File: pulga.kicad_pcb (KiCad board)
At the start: 2 copper layers, 12 parts

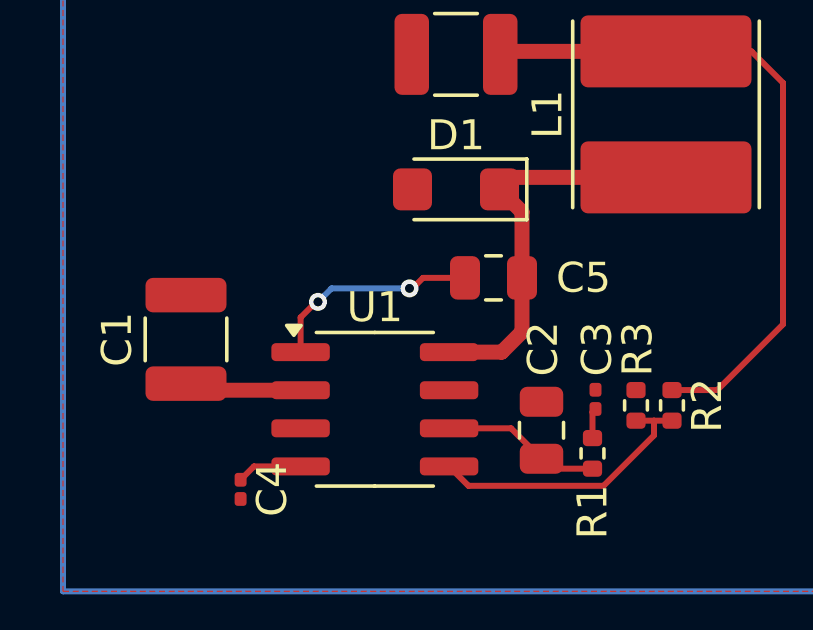
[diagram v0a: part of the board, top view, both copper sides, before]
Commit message: aumentando o caminho do GND para parte de cima do circuito
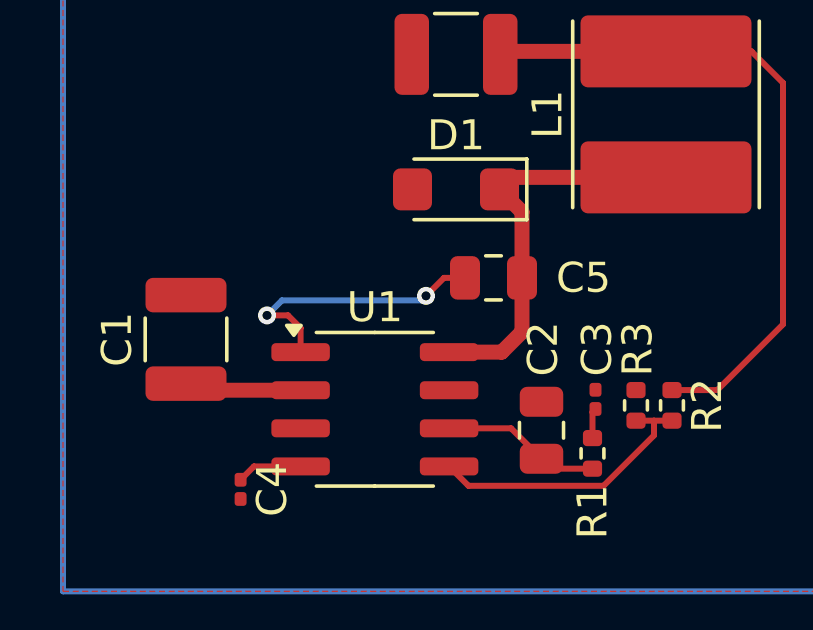
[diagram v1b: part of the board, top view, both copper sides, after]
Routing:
- net Net-(U1-BOOT): track 7.18 -> 9.43 mm
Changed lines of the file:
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@@
 	)
 	(segment
-		(start 112.82 57.27)
-		(end 112.82 58.425)
-		(width 0.2)
-		(layer "F.Cu")
-		(net 6)
-	)
-	(segment
-		(start 116.45 56.3)
-		(end 116.55 56.3)
-		(width 0.2)
-		(layer "F.Cu")
-		(net 6)
-	)
-	(segment
-		(start 113.34 56.75)
-		(end 112.82 57.27)
-		(width 0.2)
-		(layer "F.Cu")
-		(net 6)
-	)
-	(segment
-		(start 116.9 55.95)
+		(start 117.6 55.95)
 		(end 118.3 55.95)
 		(width 0.2)
@@
 	)
 	(segment
-		(start 113.4 56.75)
-		(end 113.34 56.75)
+		(start 112.4 57.2)
+		(end 112.82 57.62)
 		(width 0.2)
 		(layer "F.Cu")
@@
 	)
 	(segment
-		(start 116.55 56.3)
-		(end 116.9 55.95)
+		(start 117 56.55)
+		(end 117.6 55.95)
+		(width 0.2)
+		(layer "F.Cu")
+		(net 6)
+	)
+	(segment
+		(start 111.7 57.2)
+		(end 111.85 57.05)
+		(width 0.2)
+		(layer "F.Cu")
+		(net 6)
+	)
+	(segment
+		(start 111.7 57.2)
+		(end 112.4 57.2)
+		(width 0.2)
+		(layer "F.Cu")
+		(net 6)
+	)
+	(segment
+		(start 112.82 57.62)
+		(end 112.82 58.425)
 		(width 0.2)
 		(layer "F.Cu")
@@
 	)
 	(via
-		(at 113.4 56.75)
+		(at 111.7 57.2)
 		(size 0.6)
 		(drill 0.3)
@@
 	)
 	(via
-		(at 116.45 56.3)
+		(at 117 56.55)
 		(size 0.6)
 		(drill 0.3)
@@
 	)
 	(segment
-		(start 113.85 56.3)
-		(end 116.45 56.3)
+		(start 117 56.55)
+		(end 116.85 56.7)
 		(width 0.2)
 		(layer "B.Cu")
@@
 	)
 	(segment
-		(start 113.4 56.75)
-		(end 113.85 56.3)
+		(start 112.2 56.7)
+		(end 111.7 57.2)
 		(width 0.2)
 		(layer "B.Cu")
+		(net 6)
+	)
+	(segment
+		(start 116.85 56.7)
+		(end 112.2 56.7)
+		(width 0.2)
+		(layer "B.Cu")

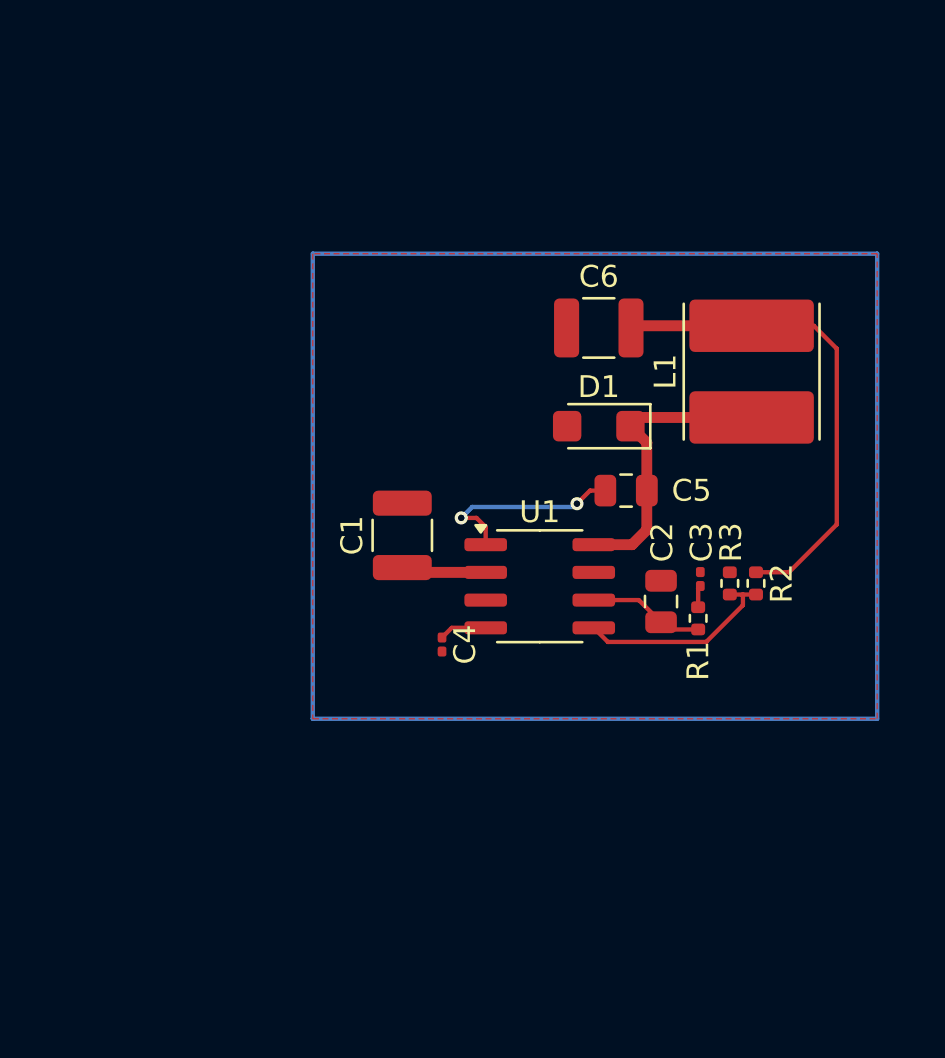
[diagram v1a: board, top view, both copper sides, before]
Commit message: criado os cortes/furas da pcb e limitando o tamanho da pcb para 38x38mm
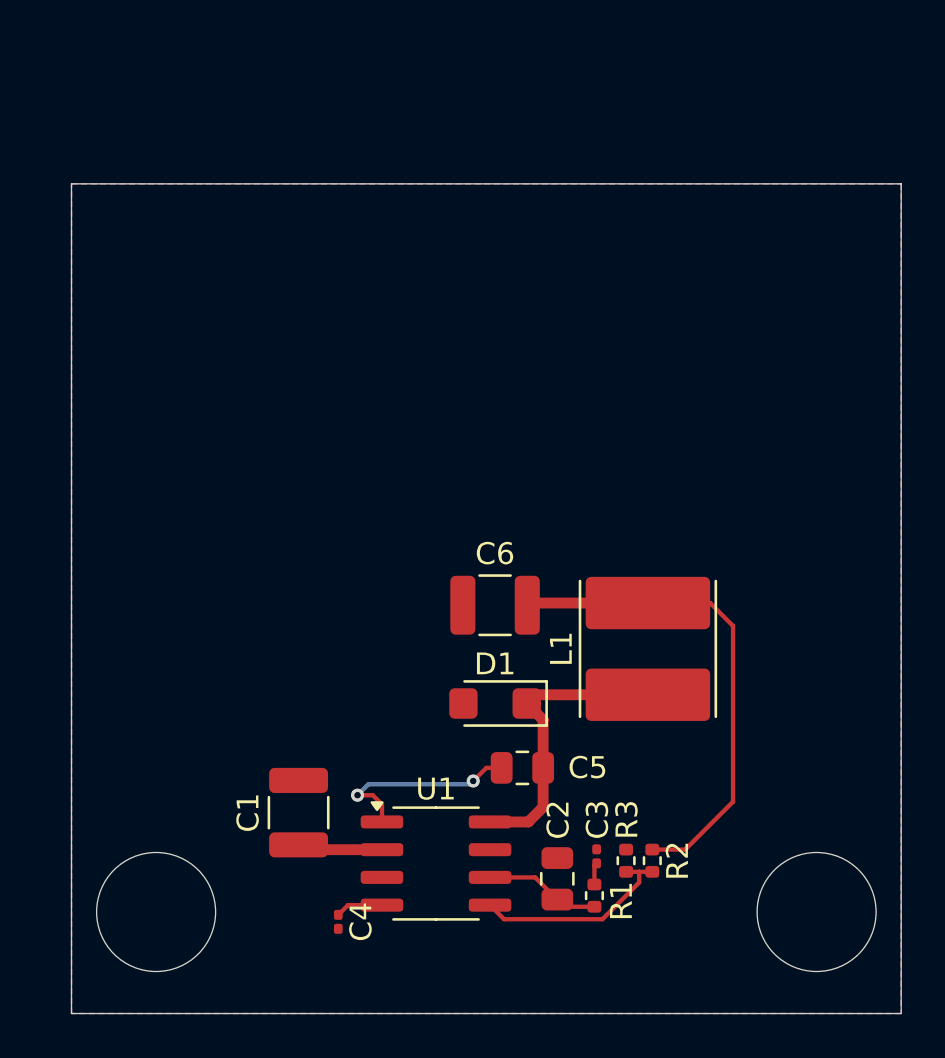
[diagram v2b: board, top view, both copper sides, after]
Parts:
- moved C1 13.6 mm to (104.2, 70.7)
- moved C2 13.6 mm to (116.1, 73.7)
- moved C3 13.6 mm to (117.9, 72.7)
- moved C4 13.6 mm to (106.1, 75.7)
- moved C5 13.6 mm to (114.5, 68.7)
- moved C6 13.6 mm to (113.2, 61.2)
- moved D1 13.6 mm to (113.2, 65.7)
- moved L1 13.6 mm to (120.2, 63.2)
- moved R1 13.6 mm to (117.8, 74.5)
- moved R2 13.6 mm to (120.5, 72.9)
- moved R3 13.6 mm to (119.2, 72.9)
- moved U1 13.6 mm to (110.5, 73.0)
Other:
- board outline added: 38 x 38 mm

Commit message: inserindo o esp32-c3 e reposicionando o circuito
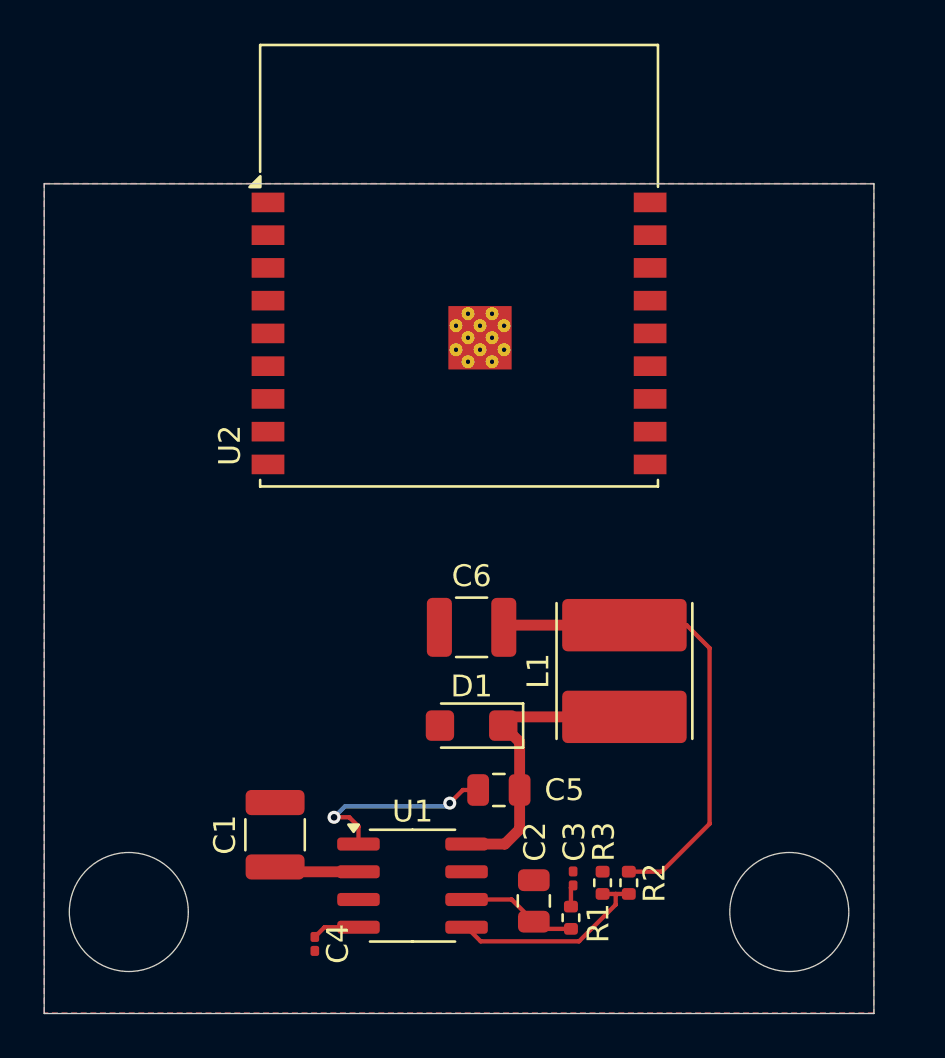
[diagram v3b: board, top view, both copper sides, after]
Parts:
- added U2: ESP32-C3-WROOM-02, RF_Module:ESP32-C3-WROOM-02, F.Cu at (111.6, 48.8)
- moved C3 1.48 mm to (116.8, 73.7)
- moved C1 1.48 mm to (103.2, 71.7)
- moved C2 1.48 mm to (115.0, 74.7)
- moved C4 1.48 mm to (105.0, 76.7)
- moved D1 1.48 mm to (112.2, 66.7)
- moved L1 1.48 mm to (119.2, 64.2)
- moved R1 1.48 mm to (116.7, 75.5)
- moved U1 1.48 mm to (109.5, 74.0)
- moved C6 1.48 mm to (112.2, 62.2)
- moved C5 1.48 mm to (113.4, 69.7)
- moved R2 1.48 mm to (119.4, 73.9)
- moved R3 1.48 mm to (118.2, 73.9)
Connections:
- net Net-(C6-Pad1) renamed 3V3

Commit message: adicionando o circuito do transceptor CAN (TCAN332GCDNR) no esquemático
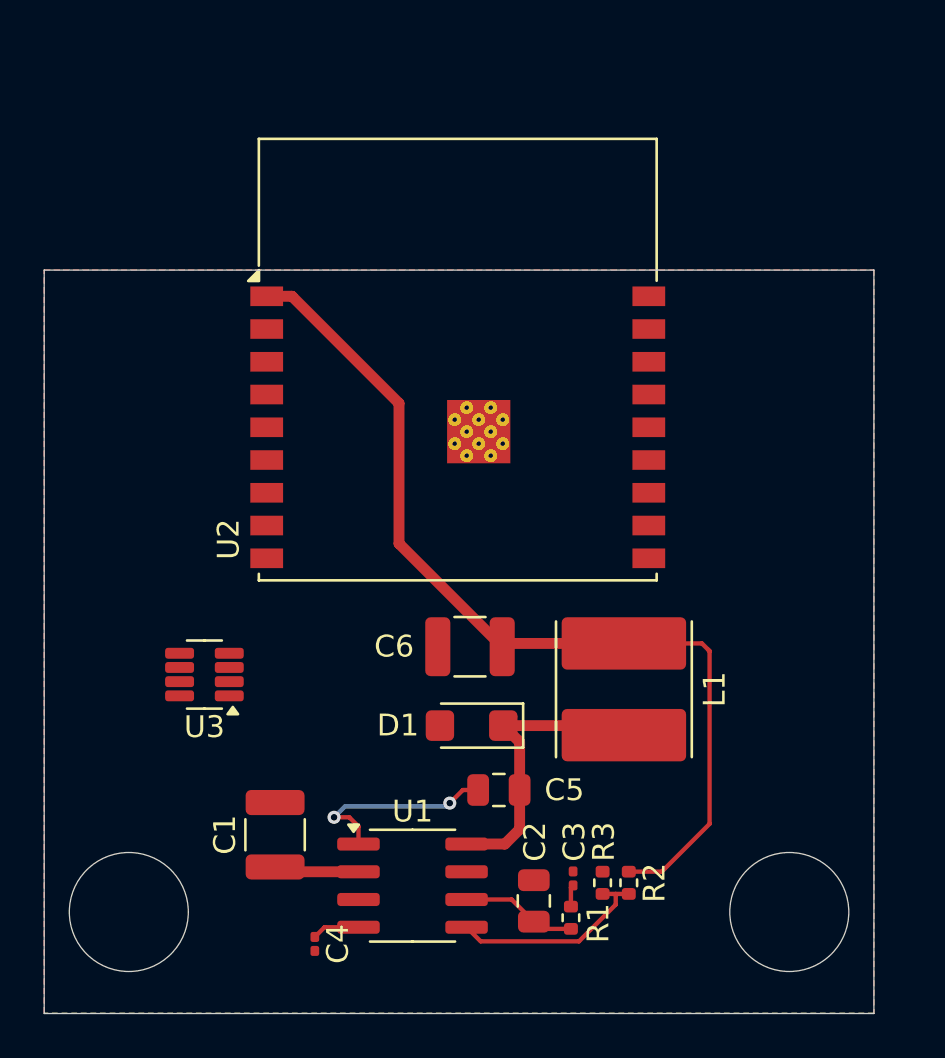
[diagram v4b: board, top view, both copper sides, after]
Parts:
- added U3: TCAN332G, Package_TO_SOT_SMD:SOT-23-8, F.Cu at (99.9, 64.4)
- moved U2 4.30 mm to (111.5, 53.0)
- moved C6 0.89 mm to (112.1, 63.1)
- moved L1 0.84 mm to (119.2, 65.0)
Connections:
- U2 pad 11: unconnected-(U2-IO20/RXD-Pad11) -> esp32_rx
- U2 pad 12: unconnected-(U2-IO21/TXD-Pad12) -> esp32_tx
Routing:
- net 3V3: track 22.6 -> 43.7 mm
- net Net-(D1-K): track 13.5 -> 14.0 mm
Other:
- board size 38 x 38 mm -> 38 x 34.1 mm

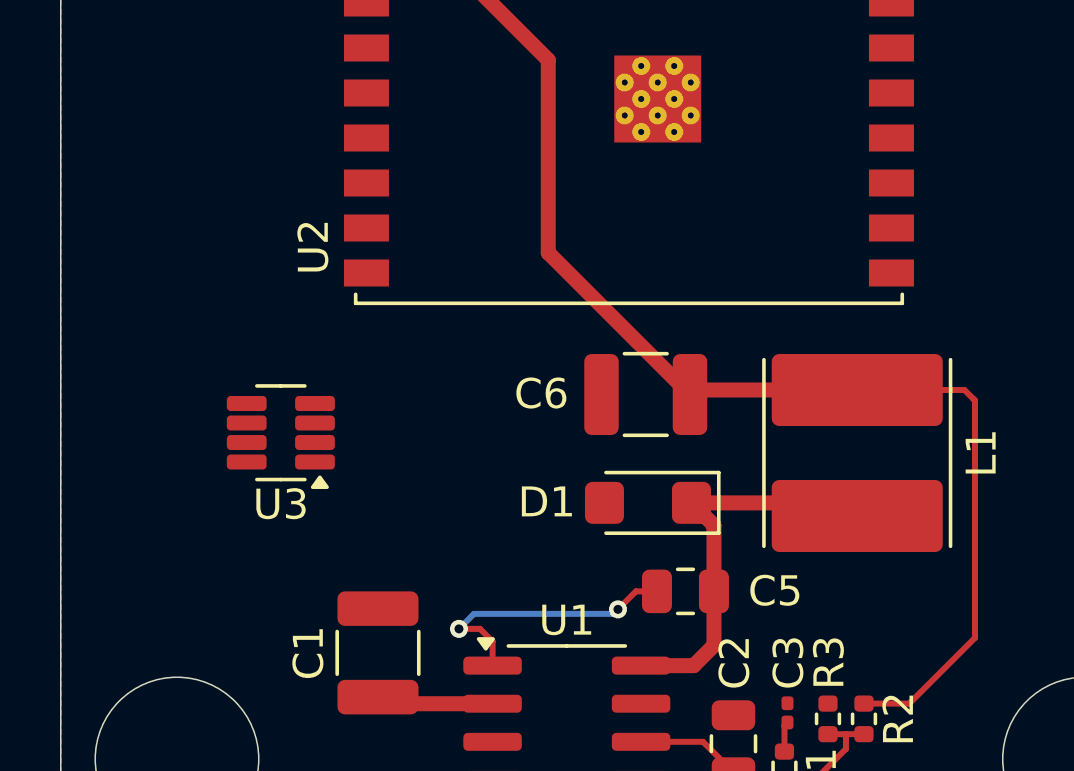
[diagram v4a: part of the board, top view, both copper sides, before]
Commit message: ligando o circuito do CAN na PCB e corrigindo o esquemático
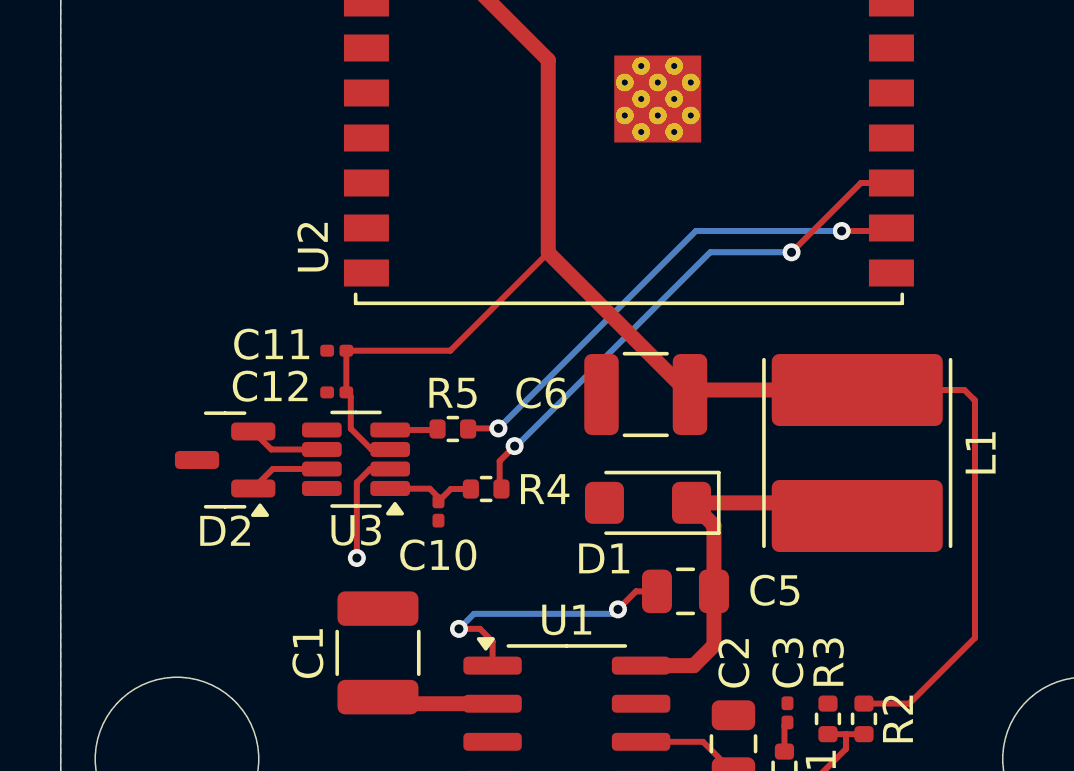
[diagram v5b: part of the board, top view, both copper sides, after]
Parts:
- added C10: 1u, Capacitor_SMD:C_0201_0603Metric, F.Cu at (105.2, 67.0)
- added C11: 1u, Capacitor_SMD:C_0201_0603Metric, F.Cu at (101.8, 61.6)
- added C12: 100u, Capacitor_SMD:C_0201_0603Metric, F.Cu at (101.8, 63.0)
- added D2: NUP2105L, Package_TO_SOT_SMD:SOT-23, F.Cu at (98.1, 65.3)
- added R4: 1k, Resistor_SMD:R_0402_1005Metric, F.Cu at (106.8, 66.2)
- added R5: 1k, Resistor_SMD:R_0402_1005Metric, F.Cu at (105.7, 64.2)
- moved U3 2.66 mm to (102.4, 65.3)
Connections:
- U3 pad 1: esp32_rx -> Net-(U3-TXD)
- U3 pad 3: 3v3 -> 3V3
- U3 pad 4: esp32_tx -> Net-(U3-RXD)
- U3 pad 6: unconnected-(U3-CANL-Pad6) -> can_l
- U3 pad 7: unconnected-(U3-CANH-Pad7) -> can_h
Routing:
- net esp32_tx: track 0.00 -> 17.9 mm, vias 0 -> 2
- net esp32_rx: track 0.00 -> 16.9 mm, vias 0 -> 2
- net 3V3: track 43.7 -> 56.0 mm
- net GND: track 0.00 -> 3.82 mm, vias 0 -> 1
- net Net-(U3-TXD): track 0.00 -> 3.12 mm
- net can_h: track 0.00 -> 2.56 mm
- net can_l: track 0.00 -> 2.54 mm
- net Net-(U3-RXD): track 0.00 -> 1.59 mm
